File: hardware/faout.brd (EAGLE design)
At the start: 100 x 70 mm, 83 parts, among them IC2 MT48LC64M4A2, Q1 12MHz, Q2 ASFL, U1 LTC3419EMS, U2 93C46B, U3 FLASH-SPI-25XXSMD1, U4 6SLX9TQG144

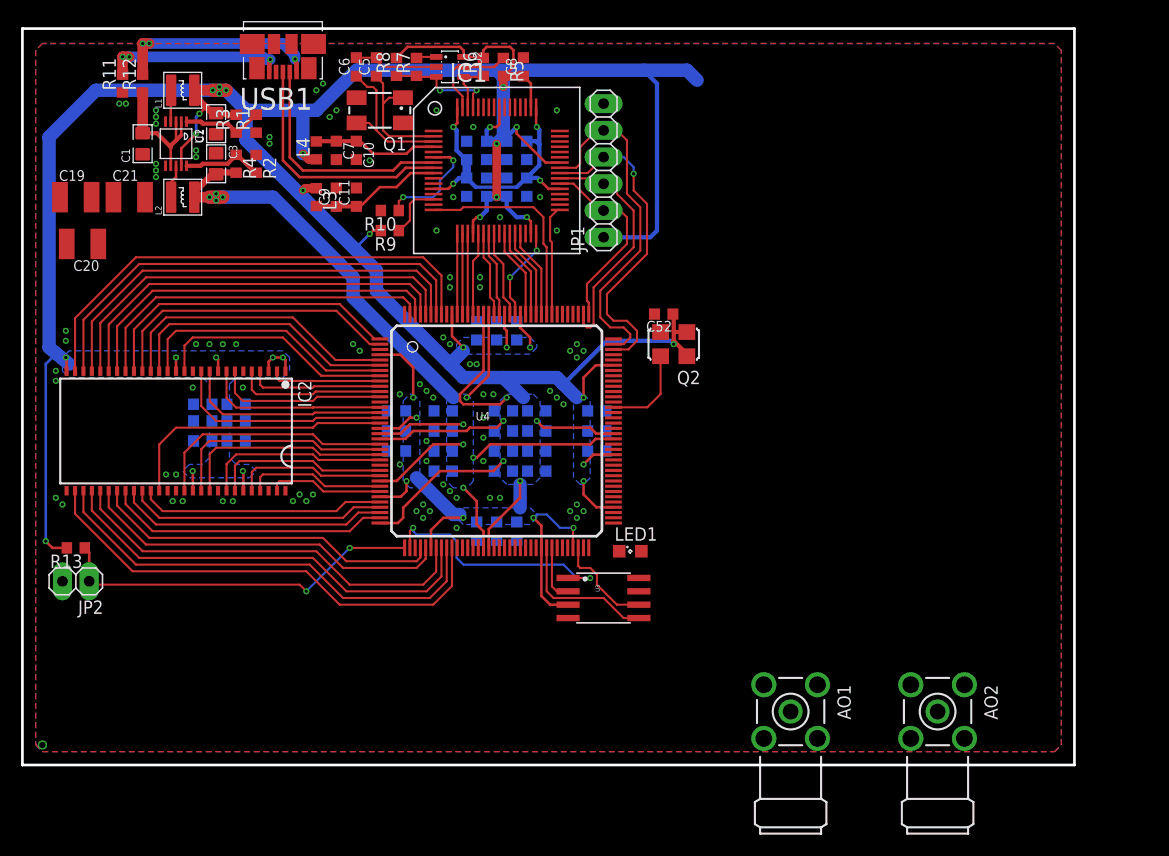
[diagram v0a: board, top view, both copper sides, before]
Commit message: Development of FAout hardware.
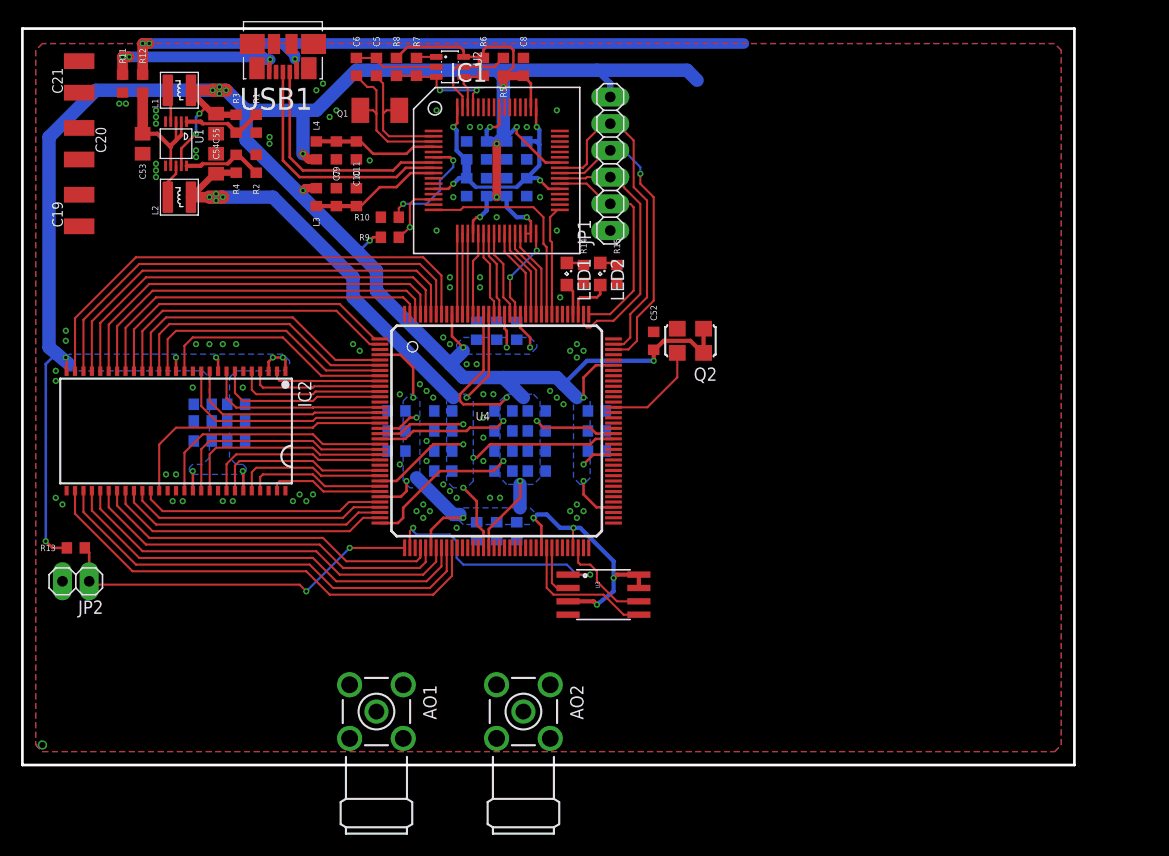
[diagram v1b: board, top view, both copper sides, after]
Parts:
- removed C1: 10u/10V, Bogdan_Commons:0805
- removed C2, C3: 22u/6V3, Bogdan_Commons:0805
- added C53: 10uF/10V, faout:R0805
- added C54, C55: 22uF/6V3, faout:R0805
- added LED2: (no value), led:SML0805
- added R14, R15: 300, faout:R0603
- C10, C11, C12, C13, C14, C15, C16, C17, C18, C22, C23, C24, C25, C26, C27, C28, C29, C30, C31, C32, C33, C34, C35, C36, C37, C38, C39, C4, C40, C41, C42, C43, C44, C45, C46, C47, C48, C49, C50, C51, C52, C7, C8, C9: device rcl:C0603K -> faout:R0603
- C5, C6: value 27pF -> 18pF; device rcl:C0603K -> faout:R0603
- L3, L4, R1, R10, R11, R12, R13, R2, R3, R4, R5, R6, R7, R8, R9: device rcl:R0603 -> faout:R0603
- Q1: device crystal:CTS406 -> faout:TXC_QUARTZ_7A
- moved AO1 39.4 mm to (33.7, 5.08)
- moved AO2 39.4 mm to (47.6, 5.08)
- moved LED1 27.0 mm to (51.8, 46.7), turned to 270 degrees
- moved C21 12.4 mm to (5.40, 65.4), turned to 90 degrees
- moved C20 9.53 mm to (5.40, 59.1), turned to 270 degrees
- moved C52 2.71 mm to (60.0, 40.3), turned to 90 degrees
- moved Q2 1.62 mm to (63.5, 40.3)
- moved C19 1.31 mm to (5.40, 52.7), turned to 90 degrees
- moved JP1 0.90 mm to (55.9, 57.1)
- moved R10 0.63 mm to (34.9, 52.1)
- moved R9 0.63 mm to (34.9, 50.2)
- moved L1 0.32 mm to (14.9, 64.1)
- moved L2 0.32 mm to (14.9, 54.0)
- moved U3 0.32 mm to (55.2, 16.2)
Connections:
- new net LED_1: LED1.A, U4.112
- new net LED_2: LED2.A, U4.111
- new net N$3: LED1.C, R14.2
- new net N$4: LED2.C, R15.2
- net 1V2: now also C55.1; no longer C3.2
- net 3V3: now also C54.1, IC1.30, JP1.6; no longer C2.2, JP1.1
- net 5V0: now also C53.1; no longer C1.2
- net GND: now also C53.2, C54.2, C55.2, JP1.1, R14.1, R15.1; no longer C1.1, C2.1, C3.1, JP1.6
- net N$2: now also Q1.2; no longer Q1.3
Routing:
- net USB_V: track 20.1 -> 64.0 mm
- net 3V3: track 422.3 -> 414.0 mm, vias 42 -> 44
- net LED_2: track 0.00 -> 4.57 mm
- net LED_1: track 0.00 -> 3.01 mm
- net TCK: track 18.6 -> 21.6 mm
- net TDI: track 23.0 -> 25.3 mm
- net TDO: track 31.2 -> 29.5 mm
- net N$3: track 0.00 -> 1.67 mm
- net N$4: track 0.00 -> 1.67 mm
- net RAM_A7: track 39.4 -> 38.1 mm
- net RAM_A5: track 43.8 -> 42.4 mm
- net RAM_A6: track 41.6 -> 40.3 mm
- net RAM_A4: track 46.0 -> 44.6 mm
- net TMS: track 33.8 -> 32.5 mm
- net CLK_IN: track 8.59 -> 9.57 mm
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
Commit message: Add DAC converters.
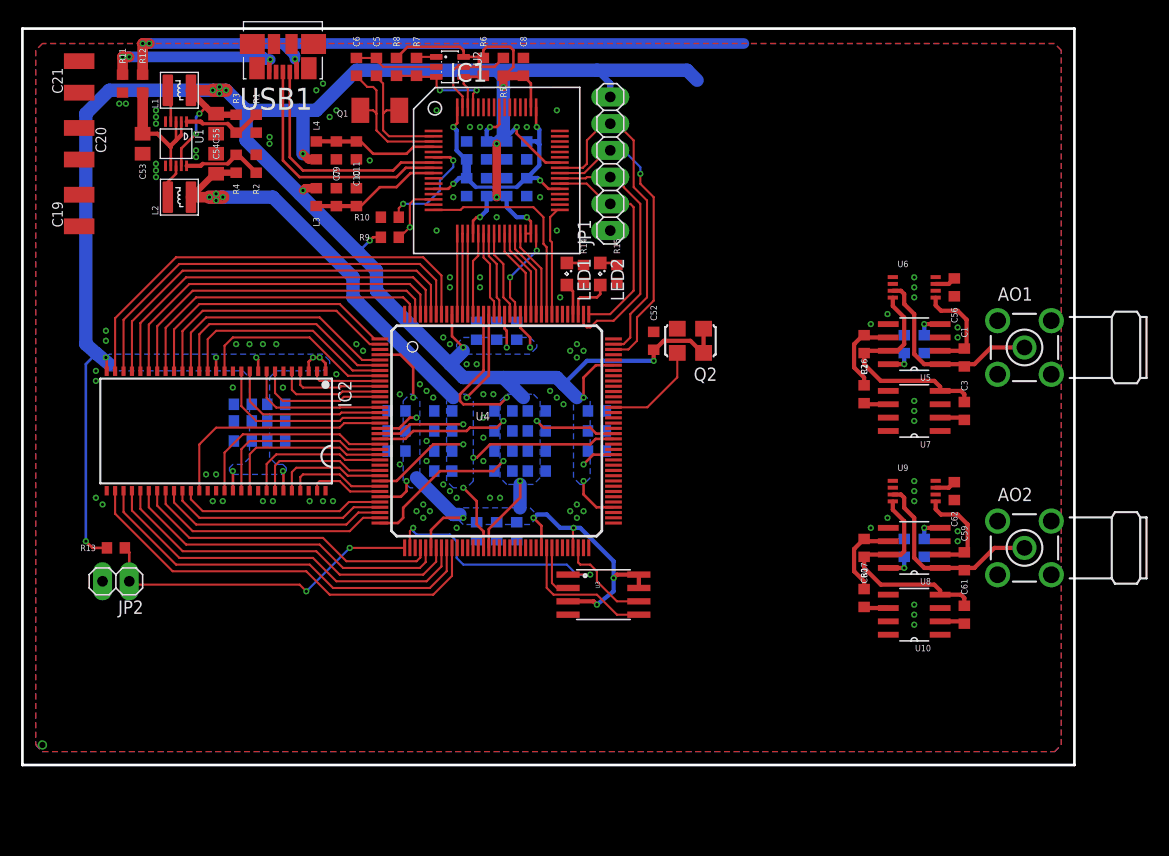
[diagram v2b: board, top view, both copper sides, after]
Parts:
- added C1, C59: 20pF, faout:R0603
- added C2, C60: 1nF, faout:R0603
- added C3, C61: 1uF?, faout:R0603
- added C56, C57, C58, C62, C63, C64: 100nF, faout:R0603
- added R16, R17: 2k, faout:R0603
- added U10, U7: REF102AU, faout:SOIC127P600X175-8N
- added U5, U8: OPA2277UA/2K5E4, faout:SOIC127P600X175-8N
- added U6, U9: DAC8811DGK, faout:MSOP-8
- moved AO1 70.7 mm to (95.2, 39.7), turned to 0 degrees
- moved AO2 50.1 mm to (95.2, 20.6), turned to 0 degrees
- moved JP2 3.81 mm to (8.89, 17.5)
- moved R13 3.81 mm to (8.89, 20.6)
- moved C46 3.81 mm to (21.0, 32.7)
- moved C47 3.81 mm to (21.0, 30.8)
- moved C48 3.81 mm to (24.1, 30.8)
- moved C49 3.81 mm to (24.1, 32.7)
- moved C50 3.81 mm to (24.1, 34.3)
- moved C51 3.81 mm to (21.0, 34.3)
- moved IC2 3.81 mm to (18.4, 31.8)
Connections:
- new net !DAC1_CS: U6.8
- new net !DAC2_CS: U9.8
- new net +15V: C57.1, C63.1, U5.8, U8.8
- new net -15V: C58.2, C64.2, U5.4, U8.4
- new net DAC1_CLK: U6.1
- new net DAC1_IOUT: C1.2, U5.2, U6.5
- new net DAC1_SDI: U6.2
- new net DAC1_VOUT: AO1.1, C1.1, U5.1, U6.3
- new net DAC1_VREF: C2.2, C3.2, U5.7, U6.4, U7.4
- new net DAC1_VREFOUT: C2.1, R16.2, U5.6
- new net DAC2_CLK: U9.1
- new net DAC2_IOUT: C59.2, U8.2, U9.5
- new net DAC2_SDI: U9.2
- new net DAC2_VOUT: AO2.1, C59.1, U8.1, U9.3
- new net DAC2_VREF: C60.2, C61.2, U10.4, U8.7, U9.4
- new net DAC2_VREFOUT: C60.1, R17.2, U8.6
- new net N$10: R16.1, U7.6
- new net N$8: R17.1, U10.6
- net 3V3: now also C3.1, C56.1, C61.1, C62.1, U10.2, U6.7, U7.2, U9.7
- net GND: now also AO1.2, AO1.3, AO1.4, AO1.5, AO2.2, AO2.3, AO2.4, AO2.5, C56.2, C57.2, C58.1, C62.2, C63.2, C64.1, U5.3, U5.5, U6.6, U8.3, U8.5, U9.6
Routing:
- net DAC2_VREF: track 0.00 -> 22.0 mm
- net DAC1_VREF: track 0.00 -> 21.8 mm
- net DAC2_VOUT: track 0.00 -> 19.2 mm
- net DAC1_VOUT: track 0.00 -> 19.0 mm
- net DAC2_IOUT: track 0.00 -> 9.55 mm
- net DAC1_IOUT: track 0.00 -> 9.47 mm
- net DAC1_VREFOUT: track 0.00 -> 8.00 mm
- net DAC2_VREFOUT: track 0.00 -> 7.94 mm
- net 3V3: track 414.0 -> 420.5 mm
- net -15V: track 0.00 -> 5.13 mm, vias 0 -> 2
- net +15V: track 0.00 -> 5.13 mm, vias 0 -> 2
- net RAM_DQMH: track 26.2 -> 22.4 mm
- net RAM_DQ6: track 21.0 -> 17.2 mm
- net RAM_A8: track 35.7 -> 31.9 mm
- net RAM_A7: track 38.1 -> 34.3 mm
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
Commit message: Connected DACs to power and FPGA.
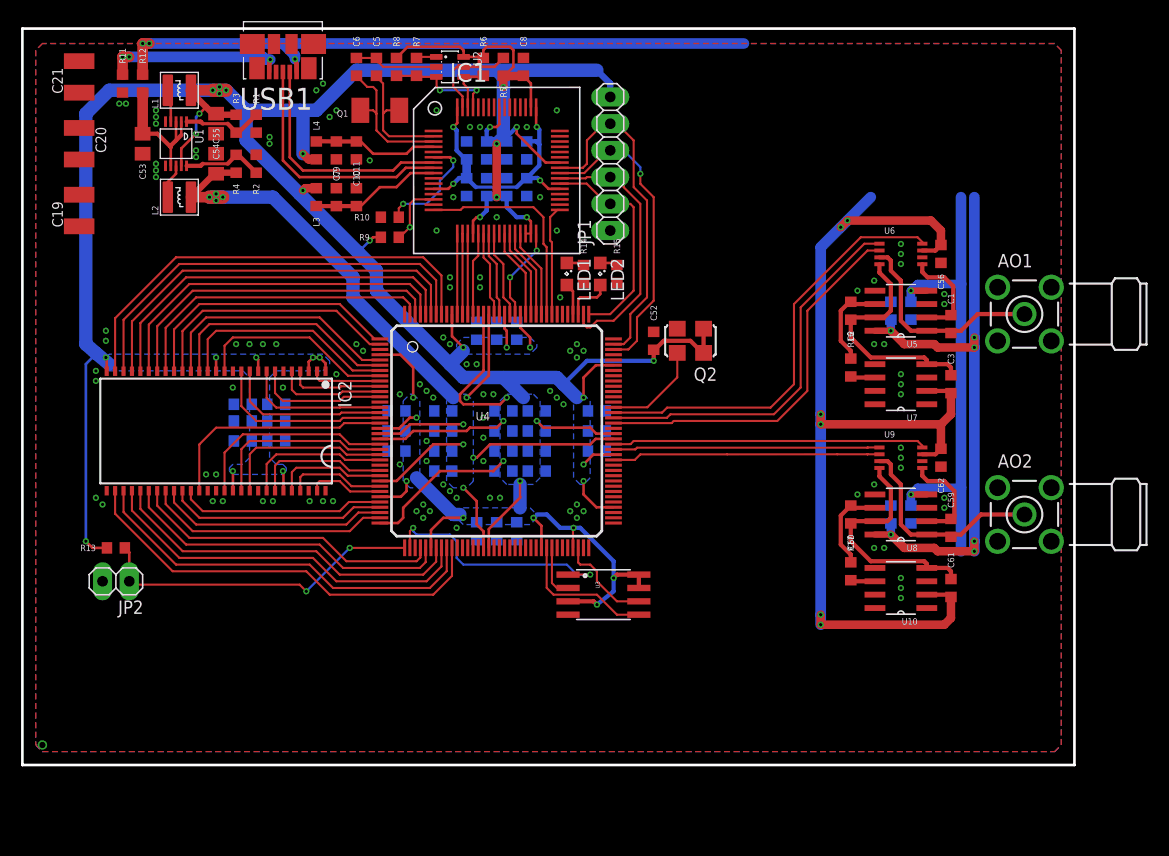
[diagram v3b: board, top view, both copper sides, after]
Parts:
- moved C60 3.42 mm to (78.7, 23.8)
- moved C2 3.42 mm to (78.7, 43.2)
- moved C59 3.42 mm to (88.3, 22.5)
- moved C62 3.42 mm to (87.3, 29.2)
- moved C63 3.42 mm to (82.5, 23.8)
- moved C64 3.42 mm to (84.5, 23.8)
- moved U8 3.42 mm to (83.5, 23.8)
- moved U9 3.42 mm to (83.5, 29.2)
- moved C1 3.42 mm to (88.3, 41.9)
- moved C56 3.42 mm to (87.3, 48.6)
- moved C57 3.42 mm to (82.5, 43.2)
- moved C58 3.42 mm to (84.5, 43.2)
- moved U5 3.42 mm to (83.5, 43.2)
- moved U6 3.42 mm to (83.5, 48.6)
- moved AO2 3.18 mm to (95.2, 23.8)
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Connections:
- net !DAC1_CS: now also U4.94
- net !DAC2_CS: now also U4.88
- net DAC1_CLK: now also U4.93
- net DAC1_SDI: now also U4.92
- net DAC2_CLK: now also U4.87
- net DAC2_SDI: now also U4.85
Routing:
- net 3V3: track 420.5 -> 498.4 mm, vias 44 -> 50
- net +15V: track 5.13 -> 57.9 mm, vias 2 -> 6
- net -15V: track 5.13 -> 48.8 mm
- net !DAC1_CS: track 0.00 -> 41.1 mm
- net DAC1_CLK: track 0.00 -> 36.6 mm
- net DAC1_SDI: track 0.00 -> 36.5 mm
- net !DAC2_CS: track 0.00 -> 29.8 mm
- net DAC2_SDI: track 0.00 -> 25.5 mm
- net DAC2_CLK: track 0.00 -> 25.4 mm
- net DAC2_VOUT: track 19.2 -> 20.4 mm
- net DAC1_VOUT: track 19.0 -> 20.3 mm
- net DAC2_VREF: track 22.0 -> 22.6 mm
- net DAC1_VREF: track 21.8 -> 22.4 mm
- net DAC2_VREFOUT: track 7.94 -> 8.57 mm
- net DAC1_VREFOUT: track 8.00 -> 8.63 mm
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
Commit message: Add parts for ADC conversion.
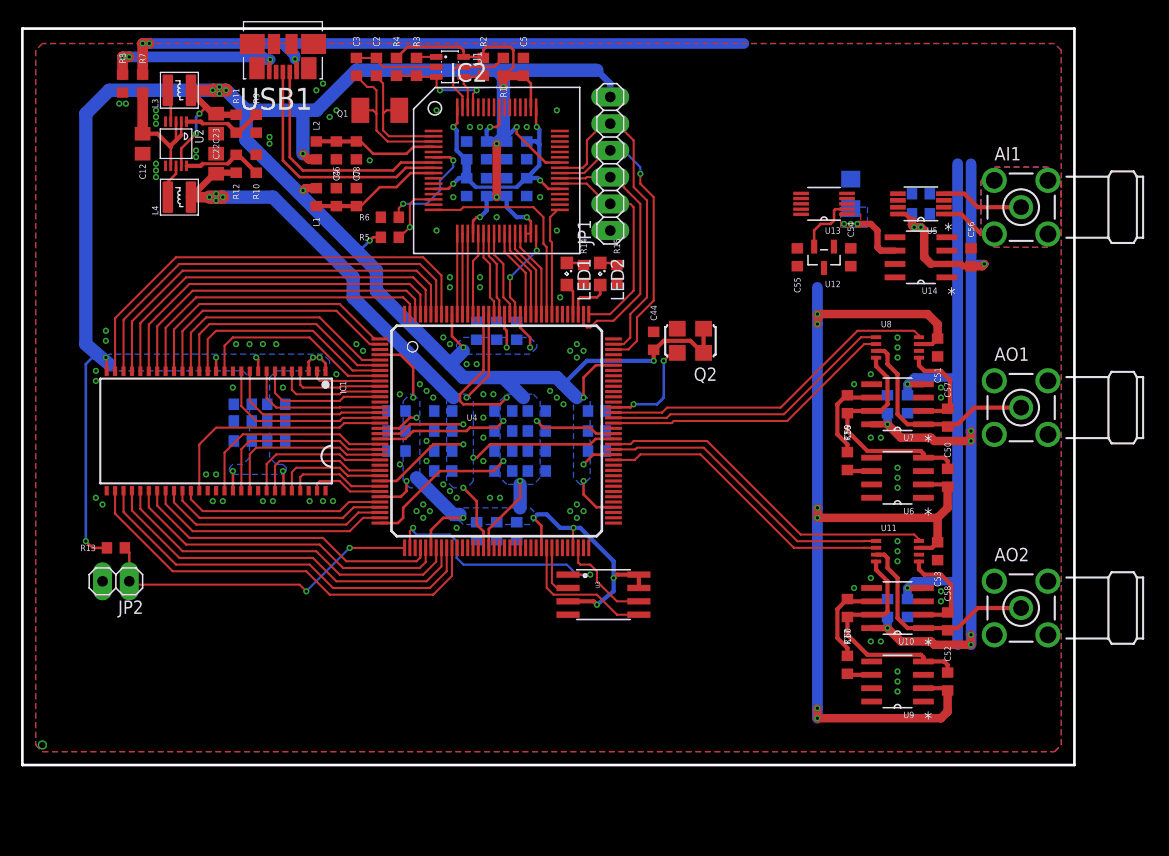
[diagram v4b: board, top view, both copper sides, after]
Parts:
- added AI1: BU-SMA, analog_out_lib:BU-SMA-H
- added C65: 22uF, resistor:C1206
- added C66, C67: 100nF, faout:R0603
- added U11: DAC8811DGK, faout:MSOP-8
- added U12: MCP1700T-2502E/TT, faout:SOT95P264X112-3N
- added U13: AD7980ARMZ, faout:SOP50P490X110-10N
- added U14: ADR435ARZ, faout:SOIC127P600X175-8N
- C1: value 20pF -> 3.3uF
- C12: value 100nF -> 10uF/10V; device faout:R0603 -> faout:R0805
- C17, C18: value 100nF -> 470nF
- C19, C20: value 100uF -> 4.7uF; device rcl:C1210K -> faout:R0603
- C2: value 1nF -> 18pF
- C21: value 100uF -> 10nF; device rcl:C1210K -> faout:R0603
- C22, C23: value 470nF -> 22uF/6V3; device faout:R0603 -> faout:R0805
- C24, C44: value 4.7uF -> 10nF
- C27, C33, C35, C37, C39, C45: value 4.7uF -> 470nF
- C28, C29, C31, C34, C38, C46: value 470nF -> 4.7uF
- C3: value 1uF? -> 18pF
- C4: value 3.3uF -> 4.7uF
- C5: value 18pF -> 100nF
- C50, C52: value 10nF -> 1uF?
- C51: value 10nF -> 100nF
- C53: value 10uF/10V -> 100nF; device faout:R0805 -> faout:R0603
- C54, C55: value 22uF/6V3 -> 1uF; device faout:R0805 -> faout:R0603
- C57, C58: value 100nF -> 20pF
- C59: value 20pF -> 1nF
- C6: value 18pF -> 4.7uF
- C61: value 1uF? -> 100nF
- C7, C9: value 4.7uF -> 100nF
- IC1: value (none) -> MT48LC64M4A2; device ftdichip-3:TQFP64-12X12 -> faout:TSOP54-400
- IC2: value MT48LC64M4A2 -> (none); device faout:TSOP54-400 -> ftdichip-3:TQFP64-12X12
- L1, L2: value 3.3uH -> (none); device Bogdan_Commons:VLS3015 -> faout:R0603
- L3, L4: value (none) -> 3.3uH; device faout:R0603 -> Bogdan_Commons:VLS3015
- R1, R2, R4: value 1K5 1% -> 10k
- R10: value 12k -> 1K5 1%
- R11: value 0 -> 6K8 1%
- R12: value 0 -> 1K5 1%
- R3: value 6K8 1% -> 2.2k
- R5: value 10k -> 1k
- R6: value 10k -> 12k
- R7: value 2.2k -> 0
- R8: value 10k -> 0
- R9: value 1k -> 1K5 1%
- U1: value LTC3419EMS -> 93C46B; device Bogdan_Commons:MSOP10 -> Bogdan_Commons:SOT23-6
- U10, U7: value REF102AU -> OPA2277UA/2K5E4
- U2: value 93C46B -> LTC3419EMS; device Bogdan_Commons:SOT23-6 -> Bogdan_Commons:MSOP10
- U5: value OPA2277UA/2K5E4 -> AD8220ARMZ; device faout:SOIC127P600X175-8N -> faout:SOP65P490X110-8N
- U6, U9: value DAC8811DGK -> REF102AU; device faout:MSOP-8 -> faout:SOIC127P600X175-8N
- U8: value OPA2277UA/2K5E4 -> DAC8811DGK; device faout:SOIC127P600X175-8N -> faout:MSOP-8
- moved C53 84.9 mm to (87.0, 20.3)
- moved C51 66.3 mm to (87.0, 39.7), flipped to the top, turned to 270 degrees
- moved C50 64.2 mm to (87.9, 27.3), flipped to the top, turned to 90 degrees
- moved C3 64.1 mm to (31.8, 66.4)
- moved C54 61.6 mm to (78.7, 48.3), turned to 90 degrees
- moved C55 56.0 mm to (73.7, 48.3), turned to 270 degrees
- moved C2 50.7 mm to (33.7, 66.4), turned to 90 degrees
- moved C1 43.6 mm to (47.9, 58.4), flipped to the bottom, turned to 270 degrees
- moved C52 42.8 mm to (87.9, 7.94)
- moved IC1 36.4 mm to (18.4, 31.8), turned to 180 degrees
- moved IC2 36.4 mm to (45.1, 56.5), turned to 270 degrees
- moved C21 36.3 mm to (24.1, 34.3), flipped to the bottom, turned to 180 degrees
- moved C20 33.9 mm to (24.1, 30.8), flipped to the bottom, turned to 180 degrees
- moved C17 33.5 mm to (21.0, 32.7), turned to 0 degrees
- moved C18 33.5 mm to (21.0, 30.8), turned to 0 degrees
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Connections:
- new net 2V5: C55.1, U12.2, U13.2
- new net ADC1_CNV: U13.6
- new net ADC1_REF: C65.1, U13.1, U14.6
- new net ADC1_SCK: U13.8
- new net ADC1_SDI: U13.9
- new net ADC1_SDO: U13.7
- new net N$11: AI1.2, AI1.3, AI1.4, AI1.5, U5.1
- new net N$12: C54.1, U12.3
- new net N$9: AI1.1, U5.4
- new net VIO: U13.10
- net !DAC1_CS: now also U8.8; no longer U6.8
- net !DAC2_CS: now also U11.8; no longer U9.8
- net !RAM_CAS: now also IC1.17; no longer IC2.17
- net !RAM_RAS: now also IC1.18; no longer IC2.18
- net !RAM_WE: now also IC1.16; no longer IC2.16
- net !USB_OE: now also IC2.33; no longer IC1.33
- net !USB_RD: now also IC2.28; no longer IC1.28
- net !USB_RESET: now also IC2.14, R5.1; no longer IC1.14, R9.1
- net !USB_RXF: now also IC2.26; no longer IC1.26
- net !USB_TXE: now also IC2.27; no longer IC1.27
- net !USB_WR: now also IC2.29; no longer IC1.29
- net +15V: now also C56.1, C61.1, C66.1, U10.8, U14.2, U7.8; no longer C57.1, U8.8
- net -15V: now also C62.2, C67.2, U10.4, U5.5, U7.4; no longer C58.2, U5.4, U8.4
- net 1V2: now also C23.1, C26.1, C28.1, C30.1, C31.1, L4.2, R12.2; no longer C34.1, C35.1, C36.1, C37.1, C55.1, L2.2, R4.2
- net 1V8: now also C1.1, C10.1, C11.1, C9.1, IC2.12, IC2.37, IC2.49, IC2.64; no longer C12.1, C13.1, C14.1, C4.1, IC1.12, IC1.37, IC1.49, IC1.64
- net 3V3: now also C13.1, C14.1, C19.1, C20.1, C21.1, C34.1, C35.1, C36.1, C37.1, C5.1, C53.1, IC1.1, IC1.14, IC1.27, IC1.3, IC1.43, IC1.49, IC1.9, IC2.20, IC2.30, IC2.31, IC2.42, IC2.50, IC2.56, L1.1, L2.1, L3.2, R1.2, R11.2, R2.2, R4.2, U1.6, U11.7, U2.9, U6.2, U8.7, U9.2; no longer C23.1, C26.1, C28.1, C3.1, C30.1, C31.1, C54.1, C56.1, C61.1, C62.1, C8.1, IC1.20, IC1.30, IC1.31, IC1.42, IC1.50, IC1.56, IC2.1, IC2.14, IC2.27, IC2.3, IC2.43, IC2.49, IC2.9, L1.2, L3.1, L4.1, R3.2, R6.2, R8.2, R9.2, U1.9, U10.2, U2.6, U6.7, U7.2, U9.7
- net 5V0: now also C12.1, R7.1, U2.2, U2.3, U2.7; no longer C53.1, R12.1, U1.2, U1.3, U1.7
- net DAC1_CLK: now also U8.1; no longer U6.1
- net DAC1_IOUT: now also C57.2, U7.2, U8.5; no longer C1.2, U5.2, U6.5
- net DAC1_SDI: now also U8.2; no longer U6.2
- net DAC1_VOUT: now also C57.1, U7.1, U8.3; no longer C1.1, U5.1, U6.3
- net DAC1_VREF: now also C50.2, C59.2, U7.7, U8.4; no longer C2.2, C3.2, U5.7, U7.4
- net DAC1_VREFOUT: now also C59.1, U7.6; no longer C2.1, U5.6
- net DAC2_CLK: now also U11.1; no longer U9.1
- net DAC2_IOUT: now also C58.2, U10.2, U11.5; no longer C59.2, U8.2, U9.5
- net DAC2_SDI: now also U11.2; no longer U9.2
- net DAC2_VOUT: now also C58.1, U10.1, U11.3; no longer C59.1, U8.1, U9.3
- net DAC2_VREF: now also C52.2, U10.7, U11.4; no longer C61.2, U10.4, U8.7
- net DAC2_VREFOUT: now also U10.6; no longer U8.6
- net EECS: now also IC2.63, R1.1, U1.5; no longer IC1.63, R5.1, U2.5
- net EEDATA: now also IC2.61, R3.1, R4.1, U1.3; no longer IC1.61, R7.1, R8.1, U2.3
- net EESK: now also IC2.62, R2.1, U1.4; no longer IC1.62, R6.1, U2.4
- net FB_1V2: now also R10.2, R12.1, U2.10; no longer R2.2, R4.1, U1.10
- net FB_3V3: now also R11.1, R9.2, U2.1; no longer R1.2, R3.1, U1.1
- net GND: now also C1.2, C19.2, C2.2, C20.2, C21.2, C3.2, C61.2, C62.1, C65.2, C66.2, C67.1, IC1.12, IC1.28, IC1.41, IC1.46, IC1.52, IC1.54, IC1.6, IC2.1, IC2.10, IC2.11, IC2.13, IC2.15, IC2.25, IC2.35, IC2.47, IC2.5, IC2.51, R10.1, R6.2, R8.1, R9.1, U1.2, U10.3, U10.5, U11.6, U12.1, U13.4, U13.5, U14.4, U2.5, U2.6, U5.6, U7.3, U7.5, U8.6; no longer C50.2, C52.2, C57.2, C58.1, C62.2, IC1.1, IC1.10, IC1.11, IC1.13, IC1.15, IC1.25, IC1.35, IC1.47, IC1.5, IC1.51, IC2.12, IC2.28, IC2.41, IC2.46, IC2.52, IC2.54, IC2.6, R1.1, R10.2, R11.1, R2.1, U1.5, U1.6, U2.2, U5.3, U5.5, U6.6, U8.3, U8.5, U9.6
- net N$1: now also C2.1, IC2.2; no longer C5.1, IC1.2
- net N$10: now also U6.6; no longer U7.6
- net N$2: now also C3.1, IC2.3; no longer C6.1, IC1.3
- net N$5: now also C4.1, IC2.4, L2.2; no longer C10.1, IC1.4, L4.2
- net N$6: now also R3.2, U1.1; no longer R7.2, U2.1
- net N$7: now also C6.1, C8.1, IC2.9, L1.2; no longer C11.1, C9.1, IC1.9, L3.2
- net N$8: now also U9.6; no longer U10.6
- net RAM_A0: now also IC1.23; no longer IC2.23
- net RAM_A1: now also IC1.24; no longer IC2.24
- net RAM_A10: now also IC1.22; no longer IC2.22
- net RAM_A11: now also IC1.35; no longer IC2.35
- net RAM_A12: now also IC1.36; no longer IC2.36
- net RAM_A2: now also IC1.25; no longer IC2.25
- net RAM_A3: now also IC1.26; no longer IC2.26
- net RAM_A4: now also IC1.29; no longer IC2.29
- net RAM_A5: now also IC1.30; no longer IC2.30
- net RAM_A6: now also IC1.31; no longer IC2.31
- net RAM_A7: now also IC1.32; no longer IC2.32
- net RAM_A8: now also IC1.33; no longer IC2.33
- net RAM_A9: now also IC1.34; no longer IC2.34
- net RAM_BA0: now also IC1.20; no longer IC2.20
- net RAM_BA1: now also IC1.21; no longer IC2.21
- net RAM_CKE: now also IC1.37; no longer IC2.37
- net RAM_CLK: now also IC1.38; no longer IC2.38
- net RAM_CS: now also IC1.19; no longer IC2.19
- net RAM_DQ0: now also IC1.2; no longer IC2.2
- net RAM_DQ1: now also IC1.4; no longer IC2.4
- net RAM_DQ10: now also IC1.45; no longer IC2.45
- net RAM_DQ11: now also IC1.47; no longer IC2.47
- net RAM_DQ12: now also IC1.48; no longer IC2.48
- net RAM_DQ13: now also IC1.50; no longer IC2.50
- net RAM_DQ14: now also IC1.51; no longer IC2.51
- net RAM_DQ15: now also IC1.53; no longer IC2.53
- net RAM_DQ2: now also IC1.5; no longer IC2.5
- net RAM_DQ3: now also IC1.7; no longer IC2.7
- net RAM_DQ4: now also IC1.8; no longer IC2.8
- net RAM_DQ5: now also IC1.10; no longer IC2.10
- net RAM_DQ6: now also IC1.11; no longer IC2.11
- net RAM_DQ7: now also IC1.13; no longer IC2.13
- net RAM_DQ8: now also IC1.42; no longer IC2.42
- net RAM_DQ9: now also IC1.44; no longer IC2.44
- net RAM_DQMH: now also IC1.39; no longer IC2.39
- net RAM_DQML: now also IC1.15; no longer IC2.15
- net SW_1V2: now also L4.1, U2.8; no longer L2.1, U1.8
- net SW_3V3: now also L3.1, U2.4; no longer L1.1, U1.4
- net TCK: now also IC2.38; no longer IC1.38
- net TDI: now also IC2.39; no longer IC1.39
- net TDO: now also IC2.40; no longer IC1.40
- net TMS: now also IC2.41; no longer IC1.41
- net USB_CLKOUT: now also IC2.32; no longer IC1.32
- net USB_D0: now also IC2.16; no longer IC1.16
- net USB_D1: now also IC2.17; no longer IC1.17
- net USB_D2: now also IC2.18; no longer IC1.18
- net USB_D3: now also IC2.19; no longer IC1.19
- net USB_D4: now also IC2.21; no longer IC1.21
- net USB_D5: now also IC2.22; no longer IC1.22
- net USB_D6: now also IC2.23; no longer IC1.23
- net USB_D7: now also IC2.24; no longer IC1.24
- net USB_DM: now also IC2.7; no longer IC1.7
- net USB_DP: now also IC2.8; no longer IC1.8
- net USB_GND: now also R8.2; no longer R11.2
- net USB_REF: now also IC2.6, R6.1; no longer IC1.6, R10.1
- net USB_V: now also R7.2; no longer R12.2
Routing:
- net +15V: track 57.9 -> 85.4 mm, vias 6 -> 9
- net -15V: track 48.8 -> 60.9 mm
- net DAC1_CLK: track 36.6 -> 28.1 mm
- net !DAC1_CS: track 41.1 -> 32.6 mm
- net DAC1_SDI: track 36.5 -> 28.1 mm
- net N$9: track 0.00 -> 7.87 mm
- net 2V5: track 0.00 -> 6.06 mm
- net N$11: track 0.00 -> 5.58 mm
- net ADC1_REF: track 0.00 -> 5.55 mm, vias 0 -> 3
- net DAC2_CLK: track 25.4 -> 28.7 mm
- net !DAC2_CS: track 29.8 -> 33.2 mm
- net DAC2_SDI: track 25.5 -> 28.9 mm
- net 3V3: track 498.4 -> 499.4 mm
- net CLK_IN: track 9.57 -> 10.3 mm, vias 0 -> 2
- added copper zone on layer 1, net ADC1_REF
- added copper zone on layer 16, net ADC1_REF
- added copper zone on layer 1, net N$11
- added copper zone on layer 16, net N$11
